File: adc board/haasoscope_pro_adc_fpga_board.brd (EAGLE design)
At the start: 224.5 x 160 mm, 638 parts, among them CN2 12Vin, IC1 ADC12DL2500ACF, IC10 TPS72325DBVR, IC13 LMH5401IRMST, IC14 LMH6401IRMZR, IC15 SN74AVC4T774PWR, IC17 DAC8562SDGSR, IC18 TLV9102IPWR, IC2 SN74AVC4T774PWR, IC21 LMH5401IRMST, IC22 TPS7A7200RGTR, IC23 TPS7A7200RGTR, IC24 TPS7A7200RGTR, IC25 TPS72325DBVR, IC26 TPS7A7200RGTR, IC27 TPS7A7200RGTR, IC28 TPS7A7200RGTR, IC29 LMH6401IRMZR, IC3 ADC122S021CIMM_NOPB, IC30 SN74AVC4T774PWR, IC33 TLV9102IPWR, IC4 TLV9102IPWR, IC5 EP4CE30F23C6N, IC6 EPCQ16ASI8N, IC7 TPS7A7200RGTR, IC8 FT232HQ, IC9 93LC56B, J1 2p-2.54, J11 8pin, J15 test1, J2 test1, J3 2p-2.54, J30 2p-2.54, J31 2p-2.54, J32 2p-2.54, J33 2p-2.54, J34 2p-2.54, J35 2p-2.54, J36 2p-2.54, J37 2p-2.54, J39 2p-2.54, J4 2p-2.54, J40 2p-2.54, J41 2p-2.54, J42 2p-2.54, J43 2p-2.54, J44 2p-2.54, J45 2p-2.54, J46 2p-2.54, K1 G6K-2F-RF-T-TR03_DC5, K2 G6K-2F-RF-T-TR03_DC5, K3 G6K-2F-RF-T-TR03_DC5, K4 G6K-2F-RF-T-TR03_DC5, K5 G6K-2F-RF-T-TR03_DC5, K6 TLP3475_TP,F, K7 TLP3475_TP,F, Q1 S8050, Q2 FDN340P, Q4 S8050, Q5 S8050, Q7 S8050, Q8 S8050, Q9 S8050, SW3 SKQGADE010, SW4 SKQGADE010, U1 WS2812-2020, U2 ADF4350BCPZ, U3 WS2812-2020, X1 USBC, Y2 OSCILLATORSMD-5X3, Y3 12MHz

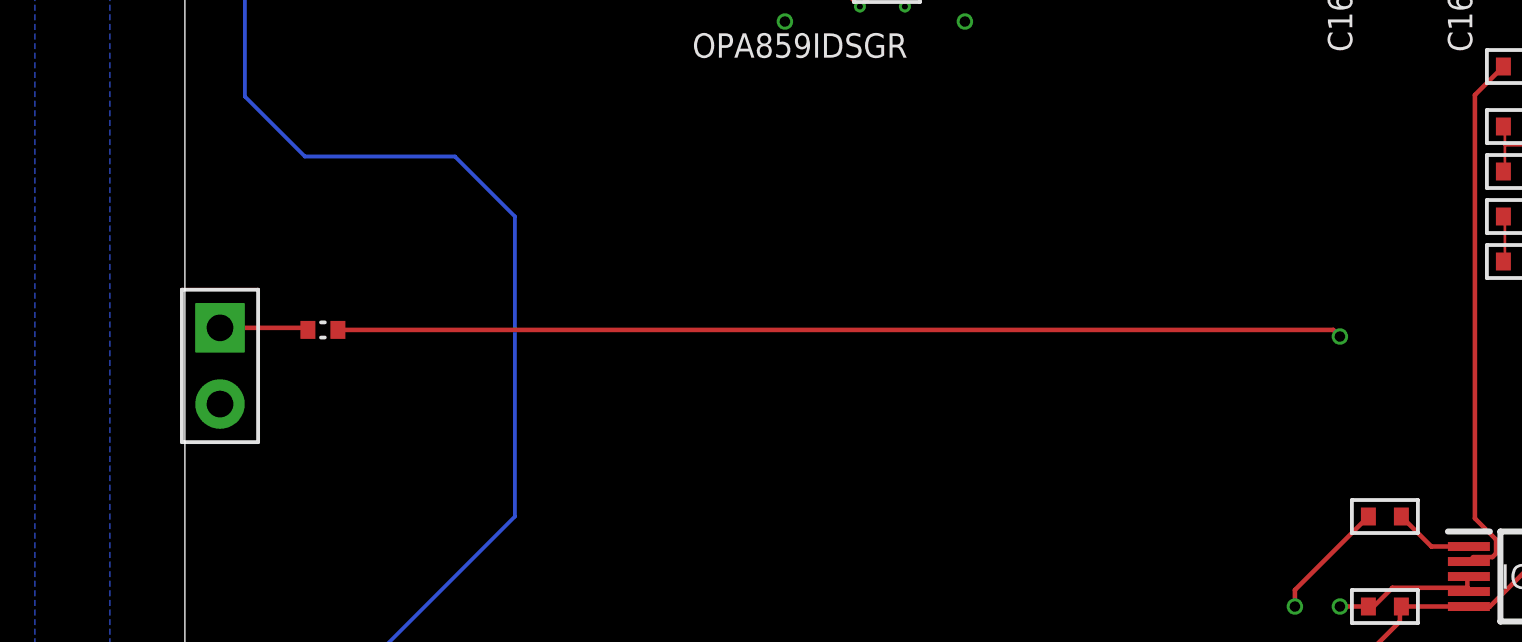
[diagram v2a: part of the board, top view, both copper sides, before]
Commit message: add 1kHzout and gnd tabs and cutouts on front panel
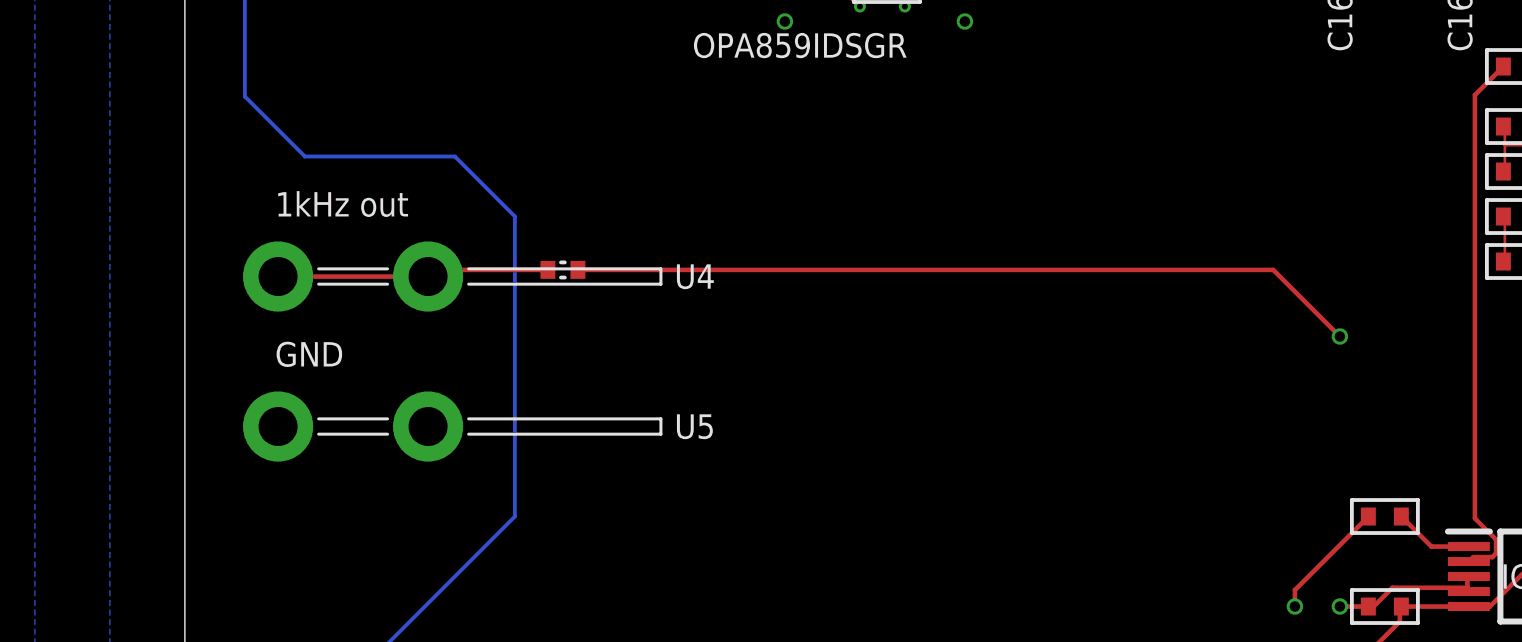
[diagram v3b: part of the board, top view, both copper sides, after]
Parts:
- removed J1: 2p-2.54, Seeed-Connector:H2-2.54
- added U4, U5: 725996-2, 725996-2:7259962
- moved R206 8.25 mm to (12.6, 113.2)
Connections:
- net 1KHZOUT: now also U4.1, U4.2; no longer J1.1
- net GND: now also U5.1, U5.2; no longer J1.2
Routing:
- net BOARDOUT3: track 179.0 -> 171.8 mm
- net 1KHZOUT: track 2.96 -> 9.08 mm
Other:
- board text added: "1kHz out"
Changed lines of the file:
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@@
 <text x="157.56" y="139.57" size="1.778" layer="21">+</text>
 <text x="209.912" y="89.229" size="0.8128" layer="21" rot="R180">5V USB</text>
+<text x="3" y="115" size="0.8128" layer="21">1kHz out</text>
+<text x="3" y="110" size="0.8128" layer="21">GND</text>
 </plain>
 <attributes>
@@
 <attribute name="VALUE" x="107.5" y="106" size="0.8128" layer="21" align="center"/>
 </element>
-<element name="R206" library="FlashPCB_Resistors" package="RES-0402" value="1k" x="4.6" y="111.22" smashed="yes">
-<attribute name="VALUE" x="3.33" y="111.72" size="0.8128" layer="27"/>
-</element>
-<element name="J1" library="Seeed-Connector" library_urn="urn:adsk.eagle:library:478" package="H2-2.54" package3d_urn="urn:adsk.eagle:package:33132/1" value="2p-2.54" x="1.17" y="110.02" smashed="yes">
-<attribute name="MPN" value="P125-1102A0BS116A1" x="1.17" y="110.02" size="1.778" layer="27" display="off"/>
+<element name="R206" library="FlashPCB_Resistors" package="RES-0402" value="1k" x="12.6" y="113.22" smashed="yes">
+<attribute name="VALUE" x="12.33" y="113.72" size="0.8128" layer="27"/>
 </element>
 <element name="R207" library="Seeed-Resistor" library_urn="urn:adsk.eagle:library:474" package="R0603" package3d_urn="urn:adsk.eagle:package:32791/1" value="NCP18WF104F03RC" x="109.5" y="98.5" smashed="yes" rot="R90">
@@
 <attribute name="VALUE" x="1.635" y="49.55336875" size="0.8128" layer="27" align="top-left"/>
 </element>
+<element name="U4" library="725996-2" package="7259962" value="725996-2" x="9" y="113" smashed="yes">
+<attribute name="DESCRIPTION" value="Contact Features: Terminal Plating Material Tin | Mating Tab Width .11 INCH | Terminal Size 2.8 | Mating Tab Width 2.79 MM | Mating Tab Thickness .02 INCH | Terminal Orientation Right Angle | PCB Terminal Type Tab | Mating Tab Thickness .51 MM | Contact Underplating Material Brass | Dimensions: Profile Height from PCB .199 INCH | PCB Thickness (Recommended) 1.57  2.36 MM | Terminal Material Thickness .51 MM | Extension Below Board 3 MM | Profile Height from PCB 5 MM | PCB Thickness (Recommended) .062 " x="9" y="113" size="0.8128" layer="27" display="off"/>
+<attribute name="HEIGHT" value="8mm" x="9" y="113" size="0.8128" layer="27" display="off"/>
+<attribute name="MANUFACTURER_NAME" value="TE Connectivity" x="9" y="113" size="0.8128" layer="27" display="off"/>
+<attribute name="MANUFACTURER_PART_NUMBER" value="725996-2" x="9" y="113" size="0.8128" layer="27" display="off"/>
+<attribute name="MOUSER_PART_NUMBER" value="571-725996-2" x="9" y="113" size="0.8128" layer="27" display="off"/>
+<attribute name="MOUSER_PRICE-STOCK" value="https://www.mouser.co.uk/ProductDetail/TE-Connectivity-AMP/725996-2?qs=qCxwlXJ4fnwSyI%252Bf7tGybA%3D%3D" x="9" y="113" size="0.8128" layer="27" display="off"/>
+<attribute name="NAME" x="17" y="113" size="0.8128" layer="25" align="center"/>
+<attribute name="VALUE" x="9" y="111" size="0.8128" layer="27" align="center"/>
+</element>
+<element name="U5" library="725996-2" package="7259962" value="725996-2" x="9" y="108" smashed="yes">
+<attribute name="DESCRIPTION" value="Contact Features: Terminal Plating Material Tin | Mating Tab Width .11 INCH | Terminal Size 2.8 | Mating Tab Width 2.79 MM | Mating Tab Thickness .02 INCH | Terminal Orientation Right Angle | PCB Terminal Type Tab | Mating Tab Thickness .51 MM | Contact Underplating Material Brass | Dimensions: Profile Height from PCB .199 INCH | PCB Thickness (Recommended) 1.57  2.36 MM | Terminal Material Thickness .51 MM | Extension Below Board 3 MM | Profile Height from PCB 5 MM | PCB Thickness (Recommended) .062 " x="9" y="108" size="0.8128" layer="27" display="off"/>
+<attribute name="HEIGHT" value="8mm" x="9" y="108" size="0.8128" layer="27" display="off"/>
+<attribute name="MANUFACTURER_NAME" value="TE Connectivity" x="9" y="108" size="0.8128" layer="27" display="off"/>
+<attribute name="MANUFACTURER_PART_NUMBER" value="725996-2" x="9" y="108" size="0.8128" layer="27" display="off"/>
+<attribute name="MOUSER_PART_NUMBER" value="571-725996-2" x="9" y="108" size="0.8128" layer="27" display="off"/>
+<attribute name="MOUSER_PRICE-STOCK" value="https://www.mouser.co.uk/ProductDetail/TE-Connectivity-AMP/725996-2?qs=qCxwlXJ4fnwSyI%252Bf7tGybA%3D%3D" x="9" y="108" size="0.8128" layer="27" display="off"/>
+<attribute name="NAME" x="17" y="108" size="0.8128" layer="25" align="center"/>
+<attribute name="VALUE" x="9" y="106" size="0.8128" layer="27" align="center"/>
+</element>
 </elements>
 <signals>
@@
 <via x="24.5" y="73.5" extent="1-16" drill="0.35"/>
 <via x="41" y="61" extent="1-16" drill="0.35"/>
-<contactref element="J1" pad="2"/>
 <contactref element="R207" pad="1"/>
 <via x="97.25" y="98.55" extent="1-16" drill="0.35"/>
@@
 <contactref element="U1" pad="2"/>
 <contactref element="U3" pad="2"/>
+<contactref element="U5" pad="2"/>
+<contactref element="U5" pad="1"/>
 </signal>
 <signal name="3V3" class="1">
@@
 <contactref element="IC5" pad="B20"/>
 <contactref element="R206" pad="P$2"/>
-<wire x1="5.1" y1="111.22" x2="38.28" y2="111.22" width="0.1524" layer="1"/>
-<wire x1="38.28" y1="111.22" x2="38.5" y2="111" width="0.1524" layer="1"/>
+<wire x1="13.1" y1="113.22" x2="36.28" y2="113.22" width="0.1524" layer="1"/>
+<wire x1="36.28" y1="113.22" x2="38.5" y2="111" width="0.1524" layer="1"/>
 <via x="38.5" y="111" extent="1-16" drill="0.35"/>
 <wire x1="38.5" y1="111" x2="97" y2="111" width="0.1524" layer="3"/>
@@
 <signal name="1KHZOUT">
 <contactref element="R206" pad="P$1"/>
-<contactref element="J1" pad="1"/>
-<wire x1="1.17" y1="111.29" x2="4.03" y2="111.29" width="0.1524" layer="1"/>
-<wire x1="4.03" y1="111.29" x2="4.1" y2="111.22" width="0.1524" layer="1"/>
+<contactref element="U4" pad="1"/>
+<contactref element="U4" pad="2"/>
+<wire x1="12.1" y1="113.22" x2="8.327" y2="113.22" width="0.1524" layer="1"/>
+<wire x1="8.327" y1="113.22" x2="8.107" y2="113" width="0.1524" layer="1"/>
+<wire x1="8.107" y1="113" x2="3.107" y2="113" width="0.1524" layer="1"/>
 </signal>
 <signal name="N$10">

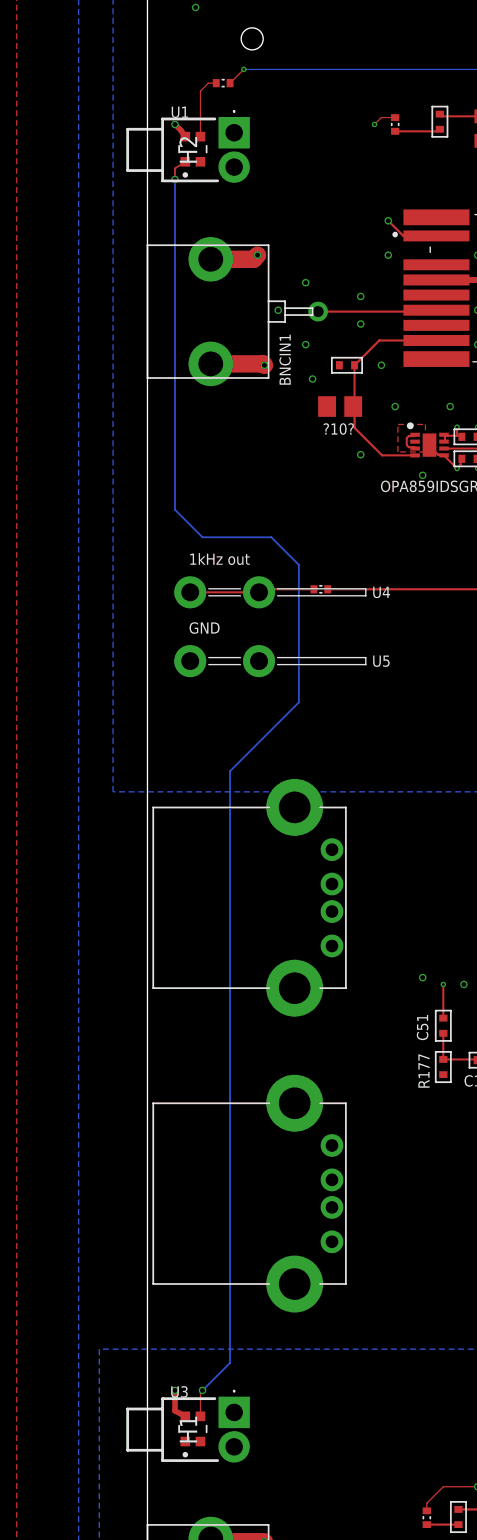
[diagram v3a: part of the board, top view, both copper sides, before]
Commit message: move leds slightly, rotate tabs
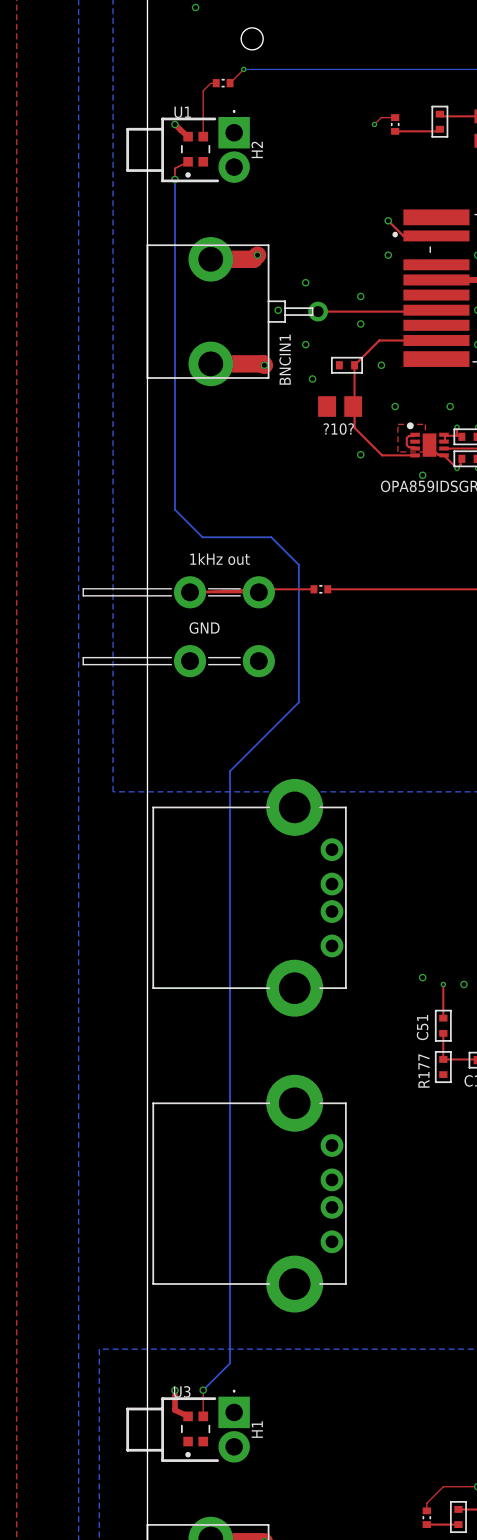
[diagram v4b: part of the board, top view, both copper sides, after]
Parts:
- moved U4 6.80 mm to (2.20, 113.0), turned to 180 degrees
- moved U5 6.80 mm to (2.20, 108.0), turned to 180 degrees
- moved U1 0.20 mm to (3.50, 145.2)
- moved U3 0.20 mm to (3.50, 52.2)
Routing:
- net 1KHZOUT: track 9.08 -> 14.0 mm

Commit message: minor, gnd vias under usbs 5v ports, to connect bottom gnd pour
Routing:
- net GND: vias 756 -> 760
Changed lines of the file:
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@@
 <setting verticaltext="up"/>
 </settings>
-<grid distance="1" unitdist="mm" unit="mm" style="lines" multiple="1" display="yes" altdistance="0.01" altunitdist="mm" altunit="mm"/>
+<grid distance="1" unitdist="mm" unit="mm" style="lines" multiple="1" display="no" altdistance="0.01" altunitdist="mm" altunit="mm"/>
 <layers>
 <layer number="1" name="top" color="12" fill="1" visible="yes" active="yes"/>
@@
 <layer number="49" name="Reference" color="7" fill="1" visible="no" active="yes"/>
 <layer number="50" name="dxf" color="7" fill="1" visible="no" active="no"/>
-<layer number="51" name="tDocu" color="7" fill="1" visible="no" active="yes"/>
-<layer number="52" name="bDocu" color="7" fill="1" visible="no" active="yes"/>
+<layer number="51" name="tDocu" color="7" fill="1" visible="yes" active="yes"/>
+<layer number="52" name="bDocu" color="7" fill="1" visible="yes" active="yes"/>
 <layer number="53" name="tGND_GNDA" color="7" fill="9" visible="no" active="no"/>
 <layer number="54" name="bGND_GNDA" color="1" fill="9" visible="no" active="no"/>
@@
 <contactref element="U5" pad="2"/>
 <contactref element="U5" pad="1"/>
+<via x="2.5" y="64.5" extent="1-16" drill="0.35"/>
+<via x="2.5" y="74.5" extent="1-16" drill="0.35"/>
+<via x="2.5" y="85.5" extent="1-16" drill="0.35"/>
+<via x="2.5" y="96.5" extent="1-16" drill="0.35"/>
 </signal>
 <signal name="3V3" class="1">
